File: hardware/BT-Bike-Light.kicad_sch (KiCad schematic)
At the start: 18 parts, among them J1 SWD_Header, J2 USB_C_Receptacle_PowerOnly_6P, J3 Conn_01x01, J4 Conn_01x01, Q1 Q_NMOS_GDS, SW1 SW_Push, U1 BC805M, U2 LIS2DTW12, U3 PAM2808, U4 BQ297xy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

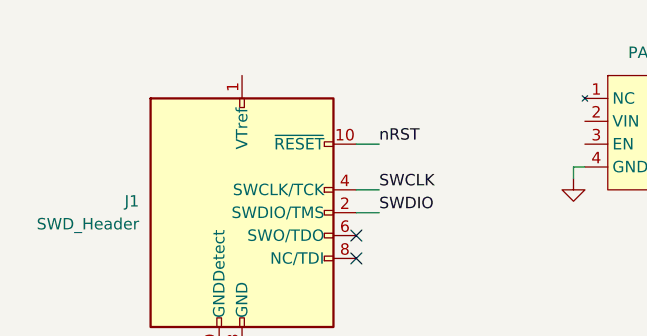
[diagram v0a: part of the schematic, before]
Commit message: Finish wiring SWD header
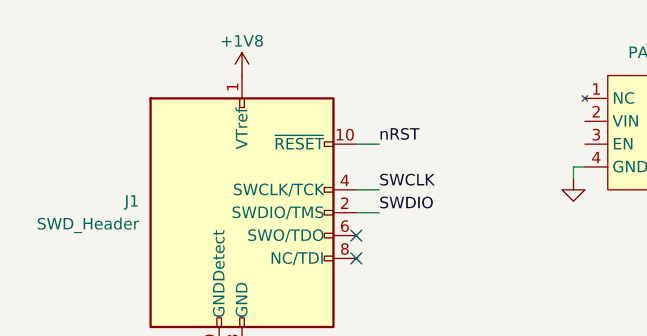
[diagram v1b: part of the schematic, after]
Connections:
- net +1V8: now also J1.1 (VTref)
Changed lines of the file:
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@@
+	)
+	(symbol
+		(lib_id "power:+1V8")
+		(at 72.39 31.75 0)
+		(unit 1)
+		(exclude_from_sim no)
+		(in_bom yes)
+		(on_board yes)
+		(dnp no)
+		(property "Reference" "#PWR010"
+			(at 72.39 35.56 0)
+			(effects
+				(font
+					(size 1.27 1.27)
+				)
+				(hide yes)
+			)
+		)
+		(property "Value" "+1V8"
+			(at 72.39 27.94 0)
+			(effects
+				(font
+					(size 1.27 1.27)
+				)
+			)
+		)
+		(property "Footprint" ""
+			(at 72.39 31.75 0)
+			(effects
+				(font
+					(size 1.27 1.27)
+				)
+				(hide yes)
+			)
+		)
+		(property "Datasheet" ""
+			(at 72.39 31.75 0)
+			(effects
+				(font
+					(size 1.27 1.27)
+				)
+				(hide yes)
+			)
+		)
+		(property "Description" "Power symbol creates a global label with name \"+1V8\""
+			(at 72.39 31.75 0)
+			(effects
+				(font
+					(size 1.27 1.27)
+				)
+				(hide yes)
+			)
+		)
+		(pin "1"
+		)
+		(instances
+			(project "BT-Bike-Light"
+				(path "/3263b444-391f-435a-aeab-6f7fca8830e2"
+					(reference "#PWR010")
+					(unit 1)
+				)
+			)
+		)
 	)
 	(symbol

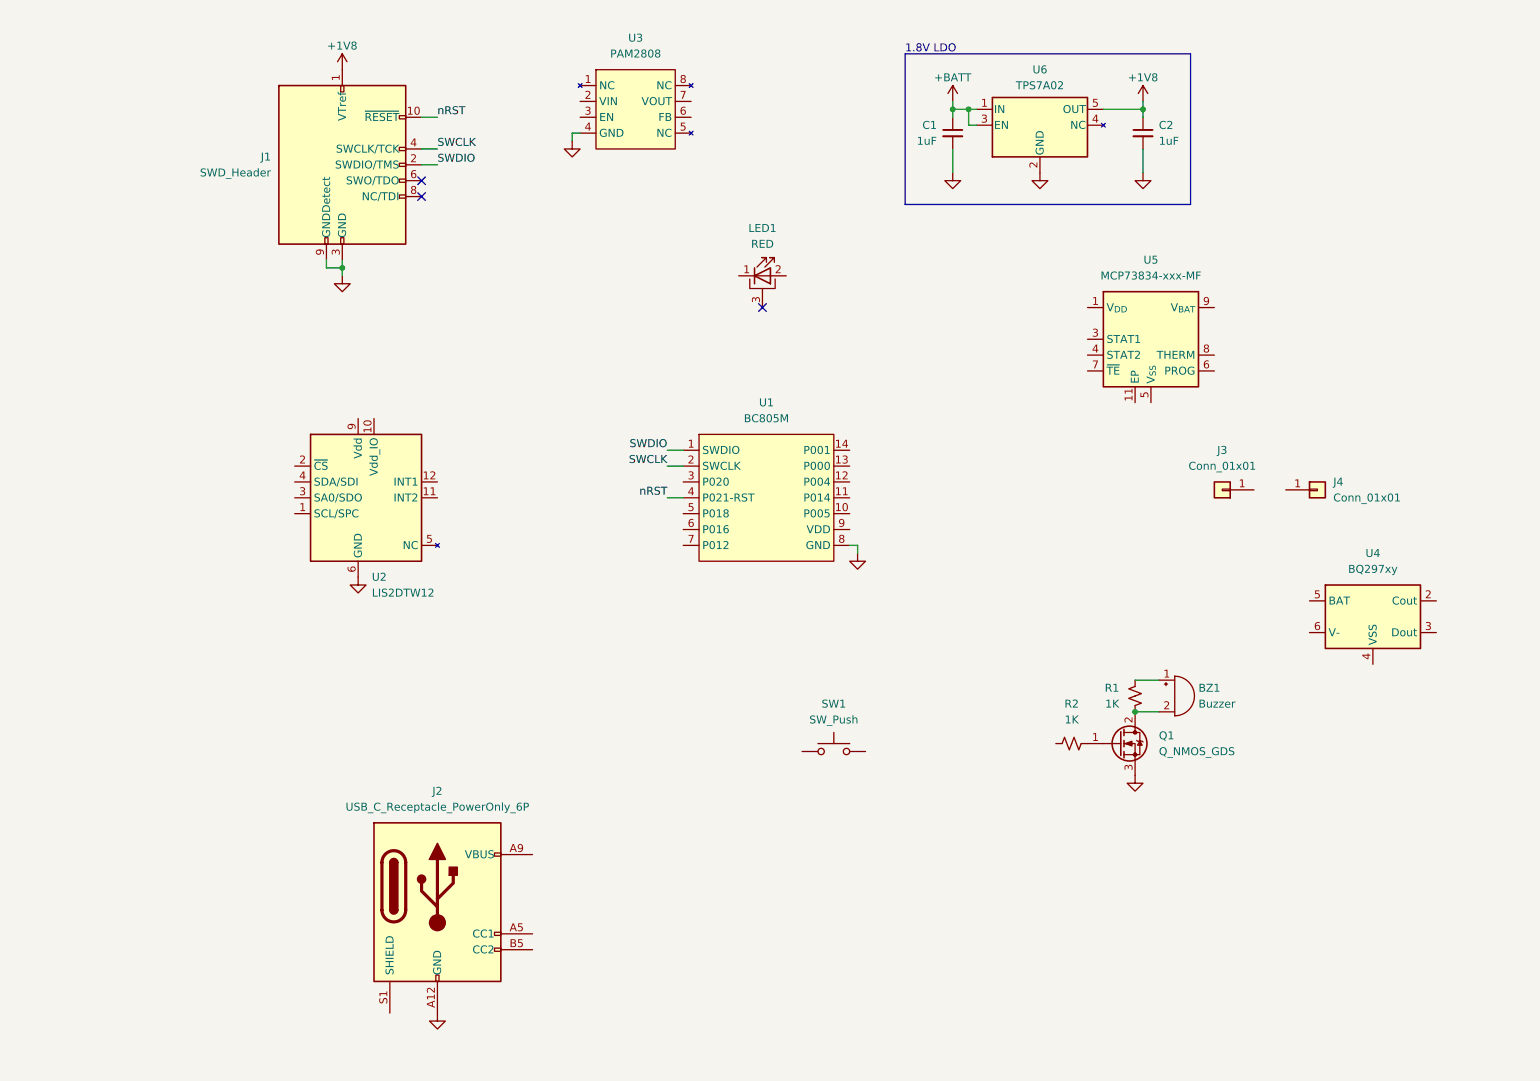
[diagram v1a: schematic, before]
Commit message: Add supporting electronics for battery charger
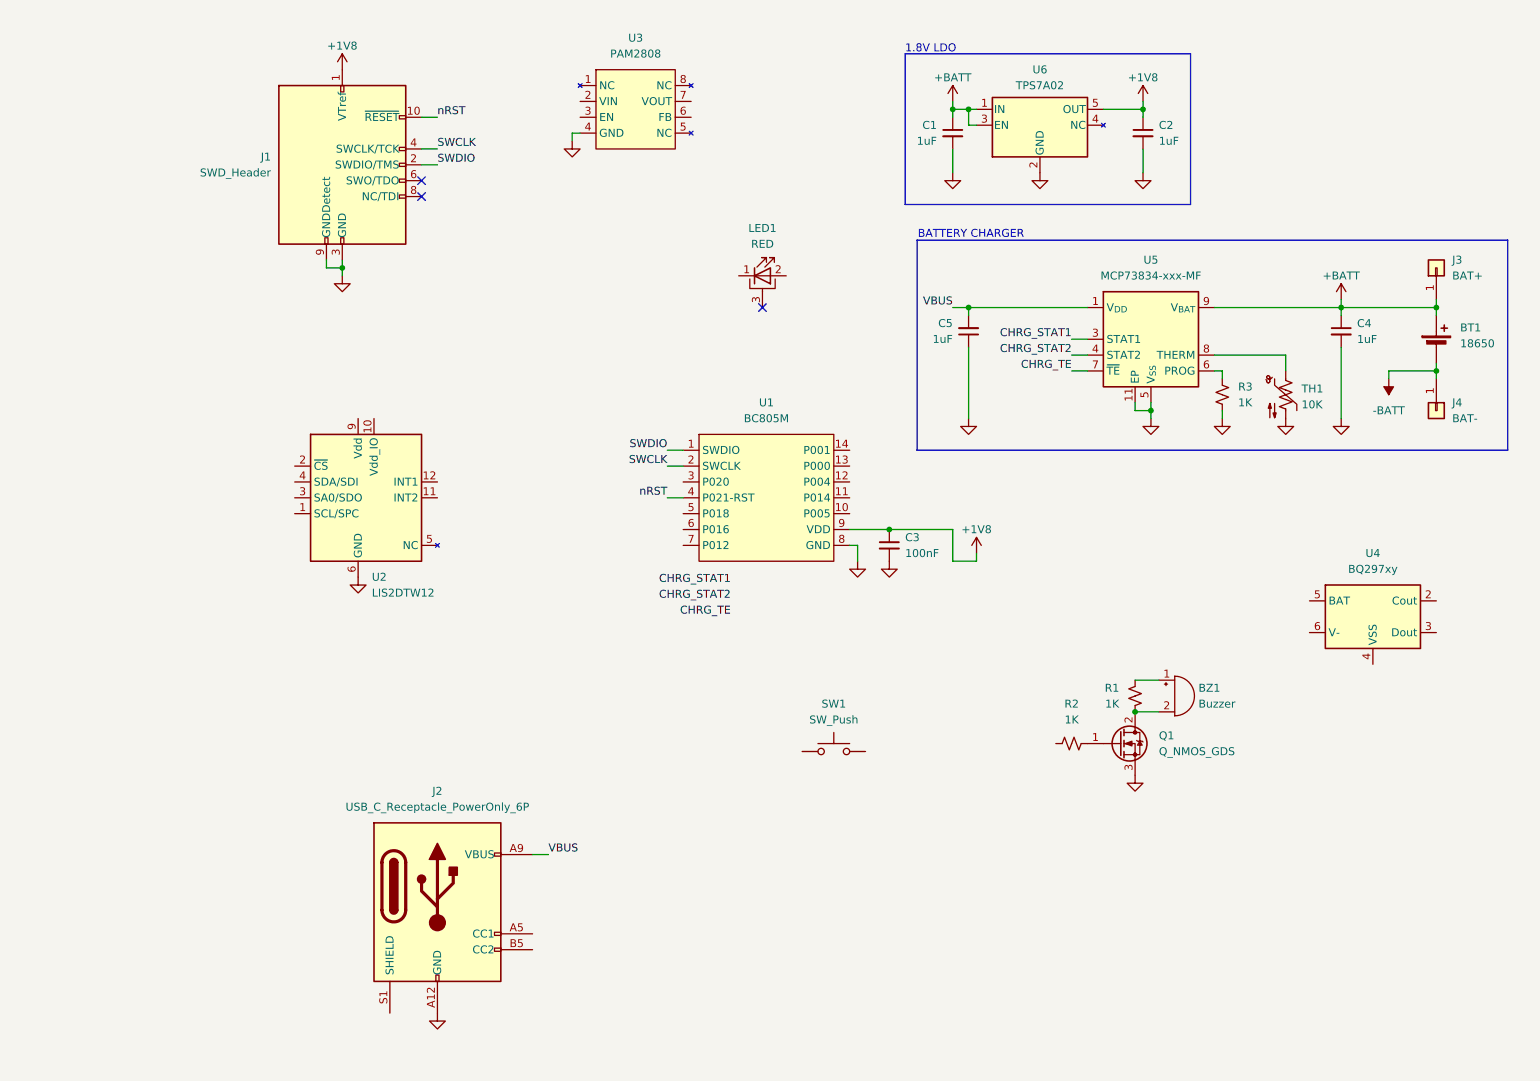
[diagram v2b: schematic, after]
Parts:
- added BT1: 18650, symbol Device:Battery_Cell
- added C3: 100nF, symbol Device:C_Small
- added C4, C5: 1uF, symbol Device:C_Small
- added R3: 1K, symbol Device:R_Small_US
- added TH1: 10K, symbol Device:Thermistor_NTC_US
- J3: value Conn_01x01 -> BAT+
- J4: value Conn_01x01 -> BAT-
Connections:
- net +1V8: now also U1.9 (VDD), C3.1
- net +BATT: now also J3.1 (Pin_1), U5.10 (V_{BAT}), U5.9 (V_{BAT}), BT1.1 (+), C4.1
- net GND: now also U5.11 (EP), U5.5 (V_{SS}), C3.2, C4.2, C5.1, R3.2, TH1.2
- net -BATT: now reaches J4.1 (Pin_1)
- net -BATT: now also BT1.2 (-)
- net VBUS: now reaches J2.A9 (VBUS), J2.B9 (VBUS)
- net VBUS: now also U5.1 (V_{DD}), U5.2 (V_{DD}), C5.2
- net CHRG_STAT1: now reaches U5.3 (STAT1)
- net CHRG_STAT2: now reaches U5.4 (STAT2)
- net at U5.6 (PROG): now also R3.1
- net CHRG_TE: now reaches U5.7 (~{TE})
- net at U5.8 (THERM): now also TH1.1
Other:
- note added: "BATTERY CHARGER"
- moved on the sheet: J3, J4

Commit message: Add supporting electronics for battery protection IC
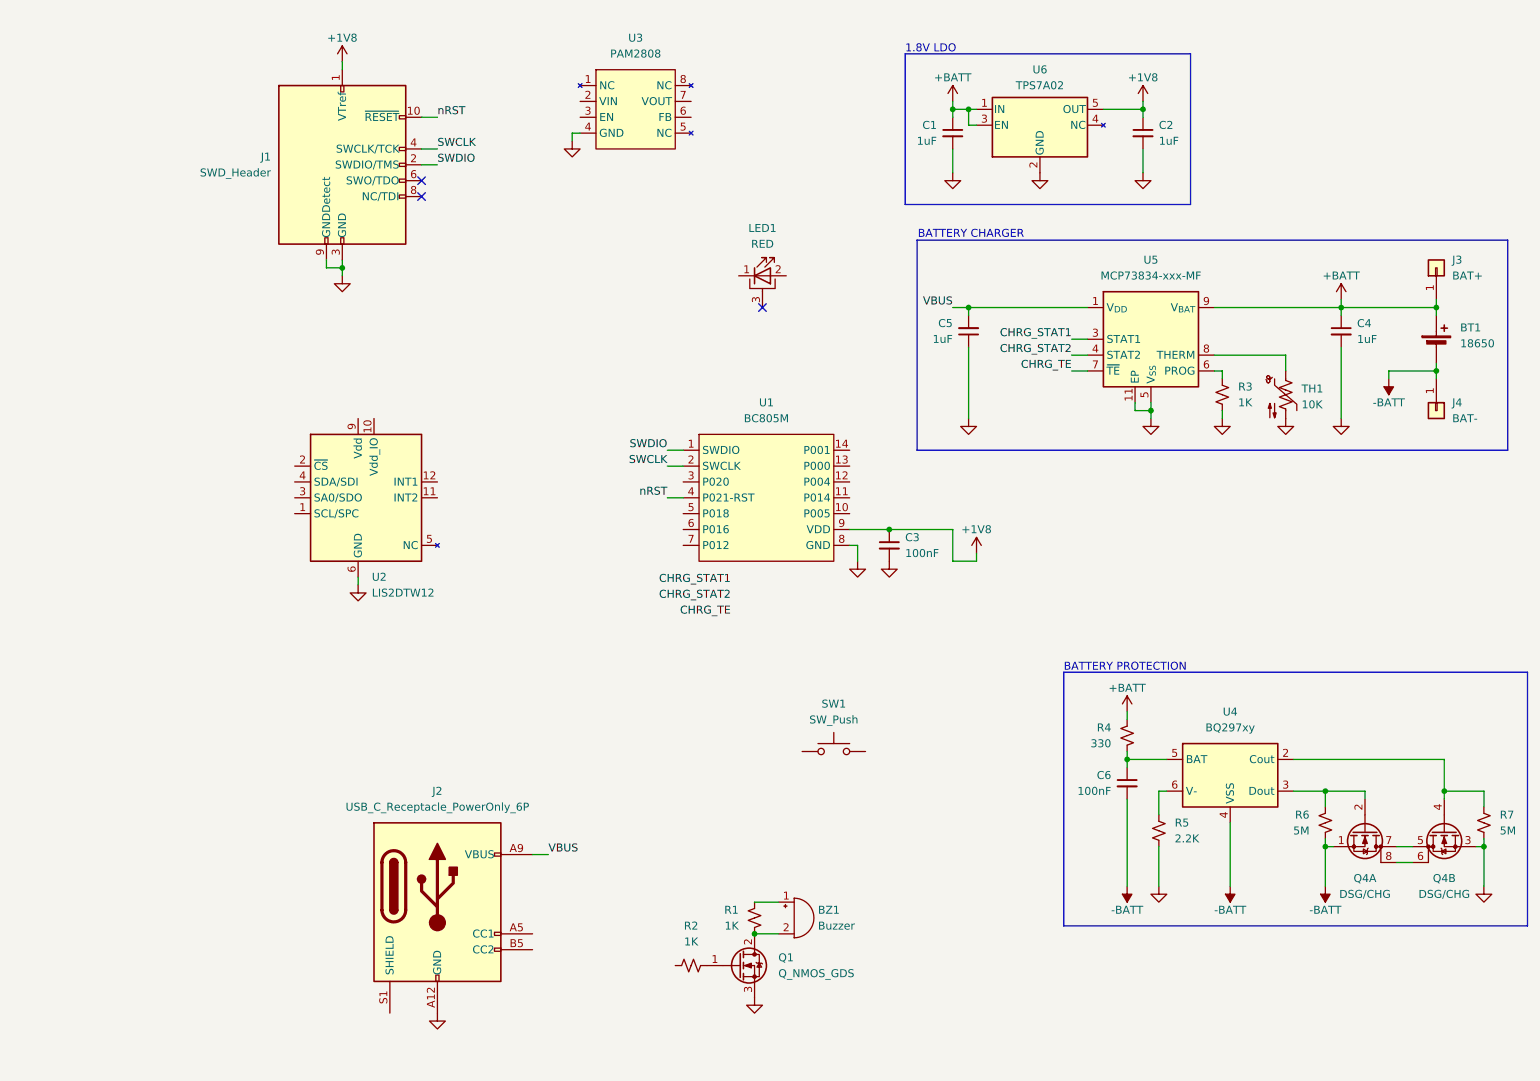
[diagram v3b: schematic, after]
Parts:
- added C6: 100nF, symbol Device:C_Small
- added Q4: DSG/CHG, Package_SO:SO-8_3.9x4.9mm_P1.27mm, symbol Device:Q_Dual_NMOS_S1G1S2G2D2D2D1D1
- added R4: 330, symbol Device:R_Small_US
- added R5: 2.2K, symbol Device:R_Small_US
- added R6, R7: 5M, symbol Device:R_Small_US
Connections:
- net +BATT: now also R4.1
- net -BATT: now also U4.4 (VSS), C6.2, Q4.1 (S), R6.2
- net GND: now also Q4.3 (S), R5.2, R7.2
- net at U4.2 (Cout): now also Q4.4 (G), R7.1
- net at U4.3 (Dout): now also Q4.2 (G), R6.1
- net at U4.5 (BAT): now also C6.1, R4.2
- net at U4.6 (V-): now also R5.1
- new net: Q4.5 (D), Q4.7 (D)
- new net: Q4.6 (D), Q4.8 (D)
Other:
- note added: "BATTERY PROTECTION"
- moved on the sheet: BZ1, Q1, R1, R2, U4

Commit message: Add supporting electronics to USB-C receptacle
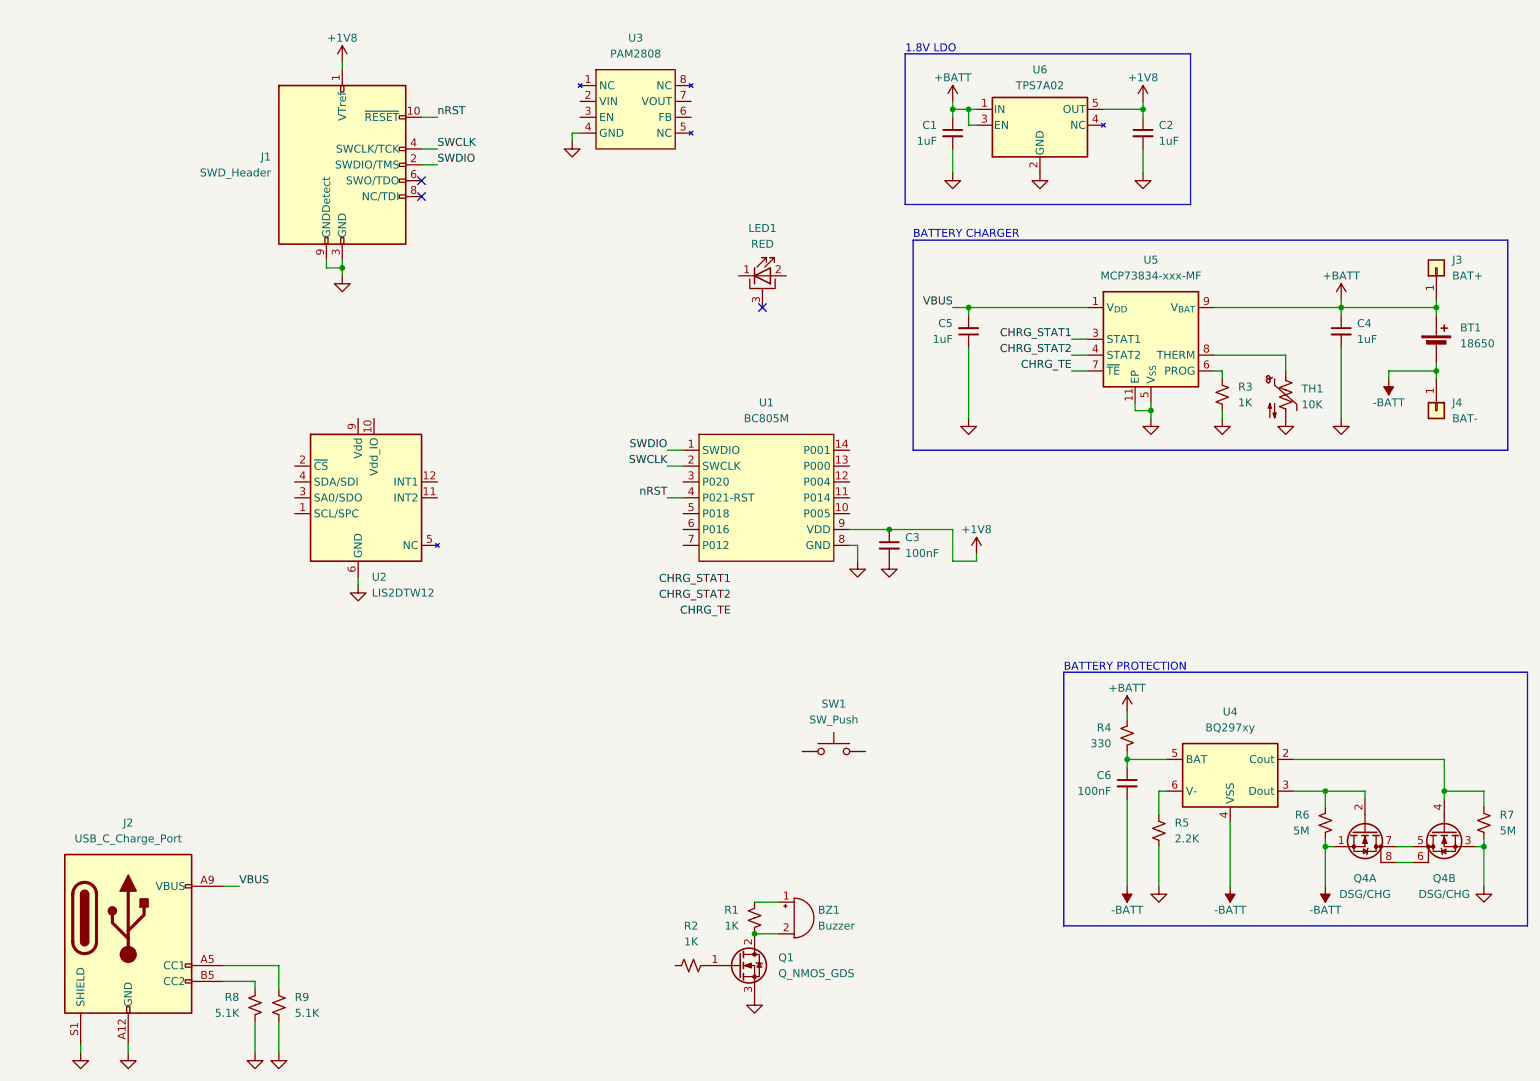
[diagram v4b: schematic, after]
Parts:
- added R8, R9: 5.1K, symbol Device:R_Small_US
- J2: value USB_C_Receptacle_PowerOnly_6P -> USB_C_Charge_Port
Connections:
- net GND: now also J2.S1 (SHIELD), R8.1, R9.1
- net at J2.A5 (CC1): now also R9.2
- net at J2.B5 (CC2): now also R8.2
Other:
- moved on the sheet: J2
